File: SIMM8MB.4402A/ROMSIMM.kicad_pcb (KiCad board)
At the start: 4 copper layers, 97.8 x 25 mm, 34 parts, among them J1 ROM, U1 MX29LV320, U10 74AHC245, U11 LD1117S33, U2 MX29LV320, U3 74AHC245, U4 74AHC245, U5 74AHC245, U6 74AHC245, U7 74AHC245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

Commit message: 8MB idk
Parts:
- added R1: 3k3, stdpads:R_0805, F.Cu at (157.1, 105.5)
- added SW1: ROM Select, Button_Switch_SMD:SW_DIP_SPSTx01_Slide_6.7x4.1mm_W8.61mm_P2.54mm_LowProfile, F.Cu at (161.3, 109.9)
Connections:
- U1 pad 13: GND -> /RA23
- U2 pad 13: GND -> /RA23
- U8 pad 11: Net-(U8-Pad11) -> GND
- U8 pad 12: Net-(U8-Pad12) -> GND
- U8 pad 13: Net-(U8-Pad13) -> GND
- U8 pad 15: Net-(U8-Pad15) -> GND
- U8 pad 17: Net-(U8-Pad17) -> GND
- U9 pad 13: Net-(U9-Pad13) -> GND
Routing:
- net /RA23: track 0.00 -> 96.6 mm, vias 0 -> 4
- net /RA2: track 109.2 -> 86.4 mm
- net GND: track 75.4 -> 78.4 mm, vias 166 -> 165
- net Net-(U9-Pad13): track 1.15 -> 0.00 mm, vias 1 -> 0
- net +3V3: track 62.7 -> 63.9 mm, vias 50 -> 51

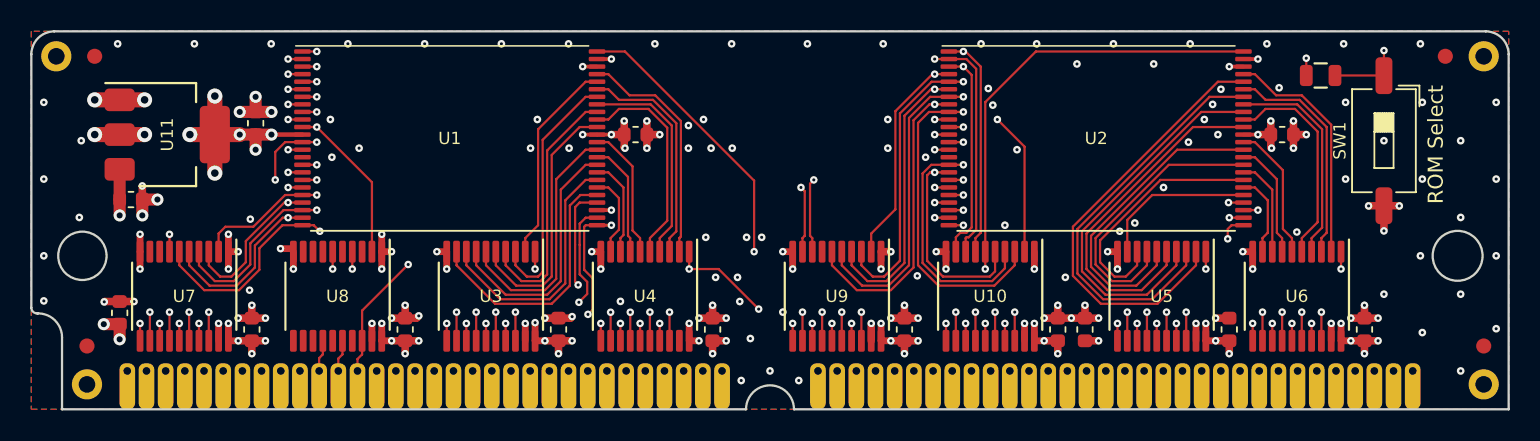
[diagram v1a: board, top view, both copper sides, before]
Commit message: 8MB SIMM as sent to JLCPCB June 2020
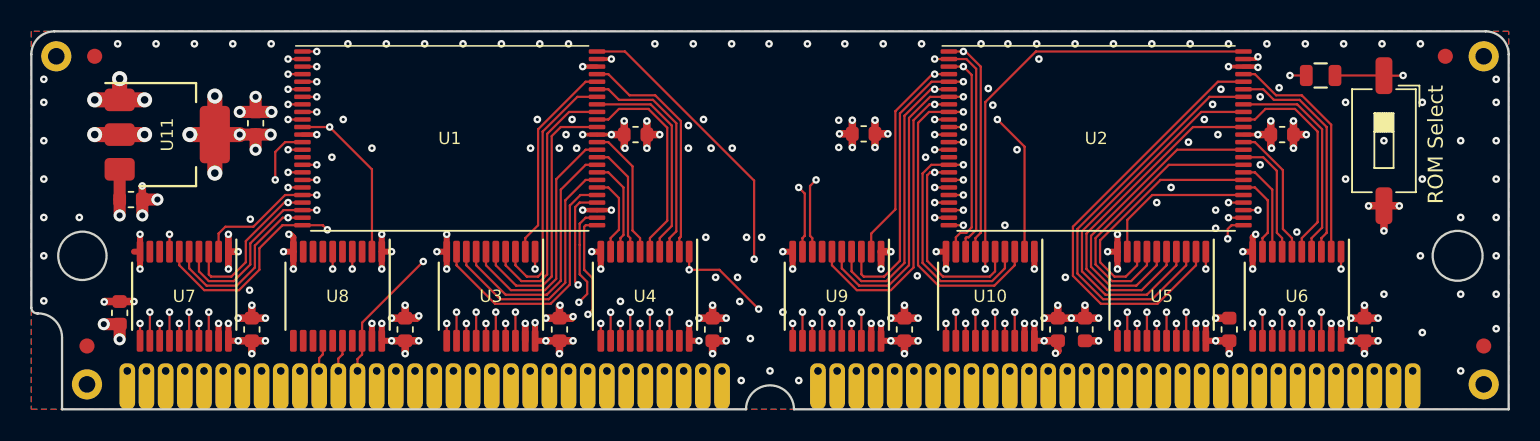
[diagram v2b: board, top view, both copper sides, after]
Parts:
- added C15: 2u2, stdpads:C_0603, F.Cu at (126.8, 109.4)
- moved C8 0.06 mm to (106.7, 122.3)
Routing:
- net GND: track 78.4 -> 90.6 mm, vias 165 -> 180
- net +3V3: track 63.9 -> 65.5 mm, vias 51 -> 77
- net /RA23: track 96.6 -> 95.0 mm, vias 4 -> 3
- net /RA2: track 86.4 -> 85.5 mm, vias 4 -> 3
- net /RD4: track 17.2 -> 18.0 mm
- net /RD5: track 16.8 -> 17.5 mm
- net /R~WE~: track 56.5 -> 56.0 mm
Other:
- rule pad_to_mask_clearance: 0.0762 -> 0.075
- rule solder_mask_min_width: 0.1524 -> 0.1

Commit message: Added probably final 8MB SIMM
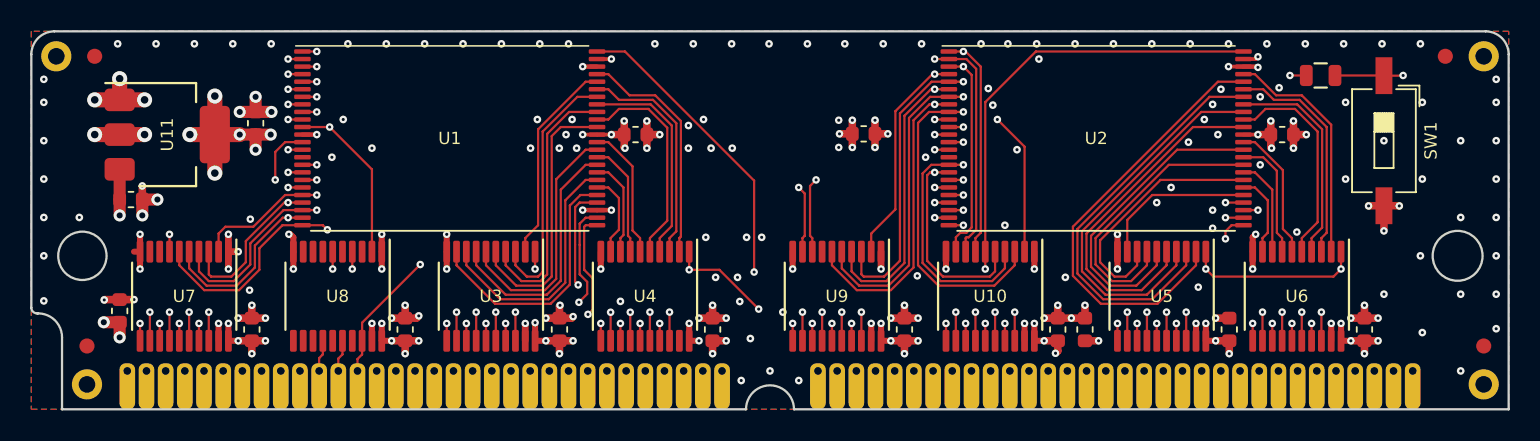
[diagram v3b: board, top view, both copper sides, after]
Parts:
- moved C1 0.13 mm to (77.6, 121.1)
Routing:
- net +5V: track 37.1 -> 123.7 mm
- net GND: track 90.6 -> 83.9 mm, vias 180 -> 171
- net /RA18: track 64.2 -> 65.3 mm

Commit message: 8MB fixes
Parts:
- added R2: 100, stdpads:R_0805, F.Cu at (118.8, 119.7)
- added U12: 74LVC1G02GW, stdpads:SOT-353, F.Cu at (97.1, 119.0)
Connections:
- U3 pad 1: /~WE~ -> /Ddir
- U4 pad 1: /~WE~ -> /Ddir
- U5 pad 1: /~WE~ -> /DdirR
- U6 pad 1: /~WE~ -> /DdirR
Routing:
- net /~WE~: track 79.2 -> 2.12 mm, vias 6 -> 0
- net /DdirR: track 0.00 -> 45.1 mm, vias 0 -> 3
- net /Ddir: track 0.00 -> 23.7 mm, vias 0 -> 3
- net /~OE~: track 2.11 -> 12.5 mm, vias 0 -> 2
- net /~CS~: track 2.10 -> 10.2 mm
- net /RA18: track 65.3 -> 63.9 mm
- net GND: track 83.9 -> 84.7 mm
- net +3V3: track 65.5 -> 66.1 mm, vias 77 -> 78
